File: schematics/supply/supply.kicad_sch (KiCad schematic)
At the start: 13 parts, among them J1 Conn_01x02_Pin, J2 Conn_01x02_Pin, J3 Conn_01x01_Pin, J4 Conn_01x01_Pin

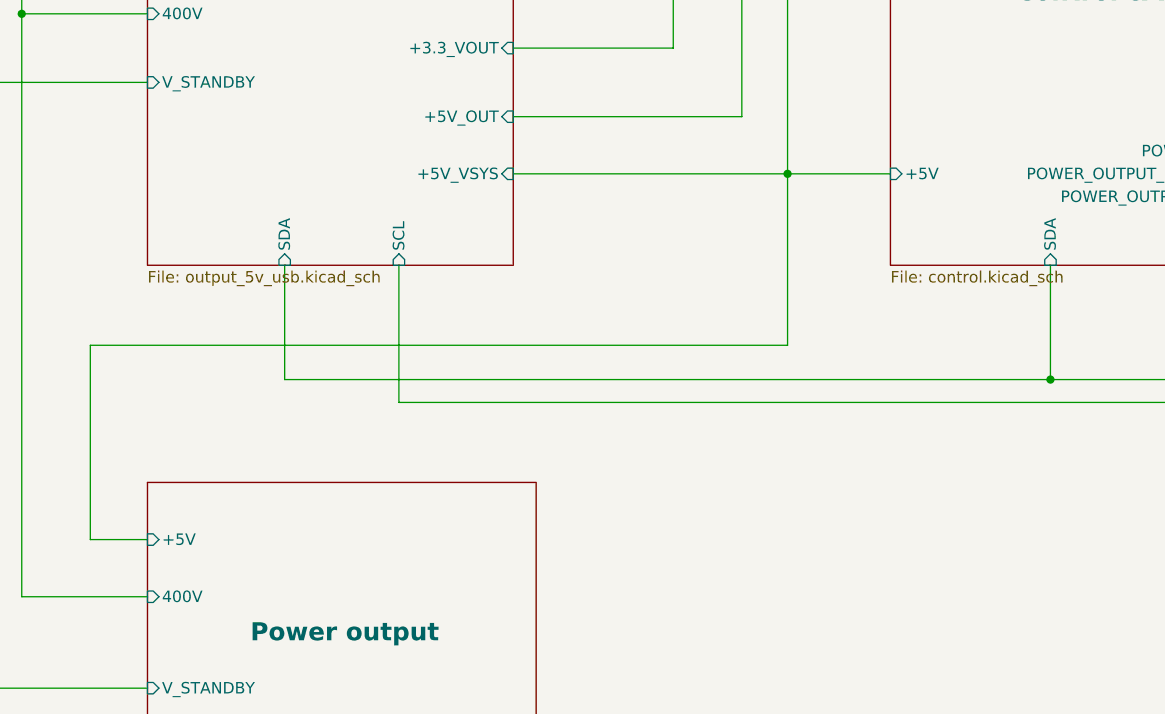
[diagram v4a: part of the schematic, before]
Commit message: Added over-voltage protection to 5V line
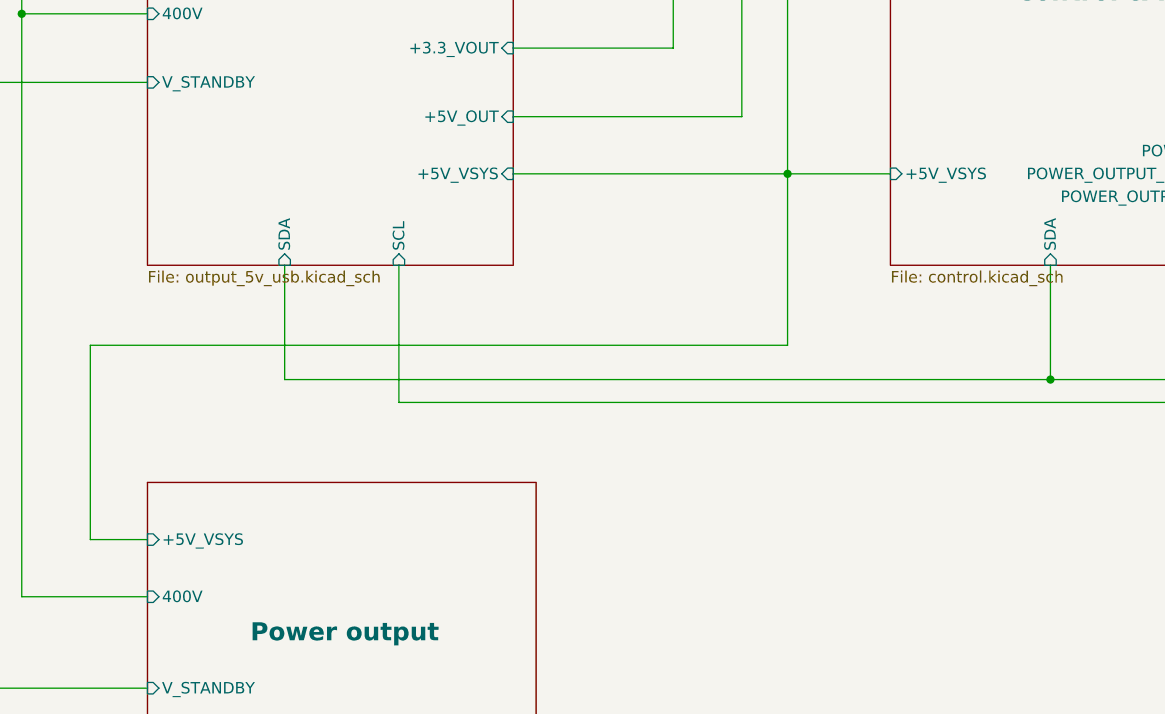
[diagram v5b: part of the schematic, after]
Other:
- sheet Control & Fan ports: added +5V_VSYS; removed +5V
- sheet Power output ports: added +5V_VSYS; removed +5V
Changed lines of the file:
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@@
-      (effects (font (size 1.27 1.27)) (justify left))
-    )
-    (pin "+5V" input (at 129.54 187.96 180)
       (effects (font (size 1.27 1.27)) (justify left))
     )
@@
     (pin "POWER_OUTPUT_FB" input (at 172.72 214.63 0)
       (effects (font (size 1.27 1.27)) (justify right))
+    )
+    (pin "+5V_VSYS" input (at 129.54 187.96 180)
+      (effects (font (size 1.27 1.27)) (justify left))
     )
     (instances
@@
       (effects (font (size 1.27 1.27)) (justify left))
     )
-    (pin "+5V" input (at 212.09 147.32 180)
-      (effects (font (size 1.27 1.27)) (justify left))
-    )
     (pin "SIGNAL_OUT" input (at 259.08 142.24 0)
       (effects (font (size 1.27 1.27)) (justify right))
@@
       (effects (font (size 1.27 1.27)) (justify right))
     )
+    (pin "+5V_VSYS" input (at 212.09 147.32 180)
+      (effects (font (size 1.27 1.27)) (justify left))
+    )
     (instances

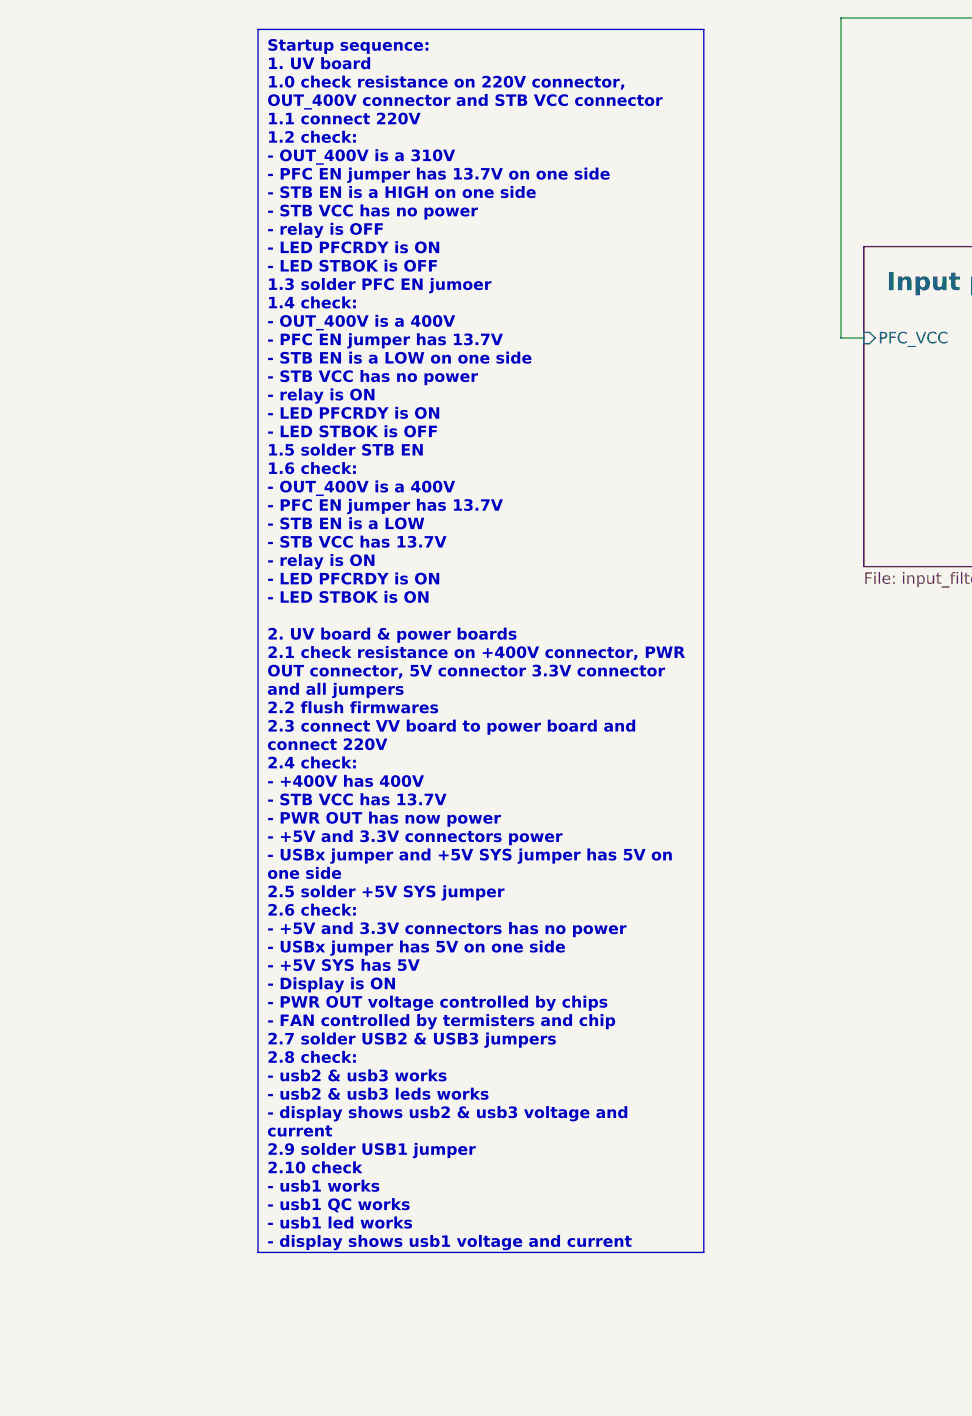
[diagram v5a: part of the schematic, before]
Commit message: Fixed problem with 20V on one leg of comparator
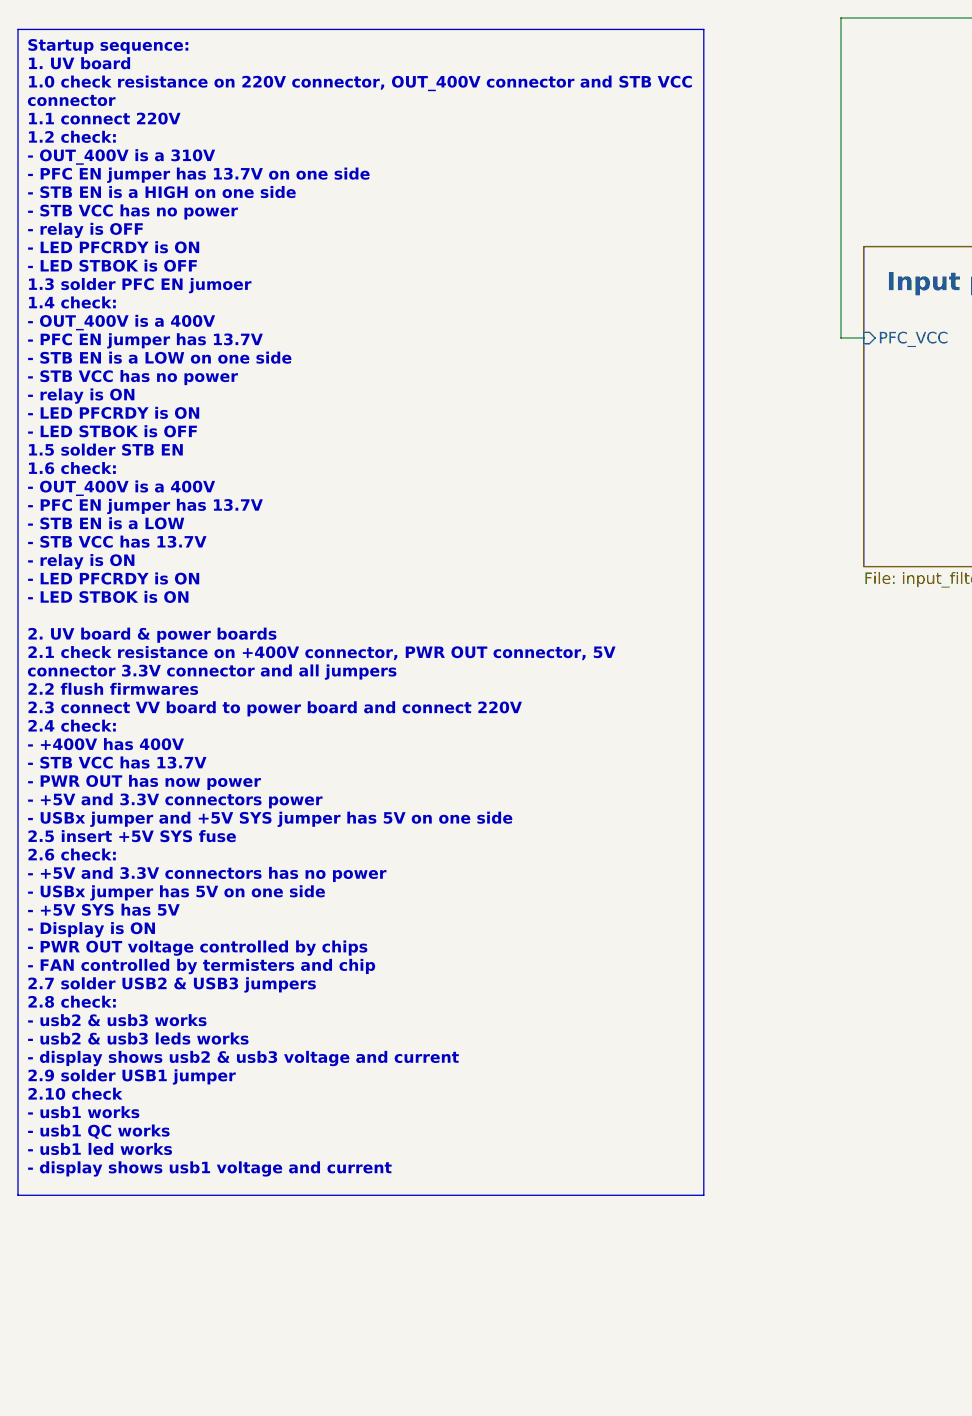
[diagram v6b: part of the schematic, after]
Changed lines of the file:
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@@
     (stroke (width 0) (type default))
   )
-  (text_box "Startup sequence:\n1. UV board\n1.0 check resistance on 220V connector, OUT_400V connector and STB VCC connector\n1.1 connect 220V\n1.2 check: \n    - OUT_400V is a 310V\n    - PFC EN jumper has 13.7V on one side \n    - STB EN is a HIGH on one side\n    - STB VCC has no power\n    - relay is OFF\n    - LED PFCRDY is ON\n    - LED STBOK is OFF\n1.3 solder PFC EN jumoer\n1.4 check:\n    - OUT_400V is a 400V\n    - PFC EN jumper has 13.7V\n    - STB EN is a LOW on one side\n    - STB VCC has no power\n    - relay is ON\n    - LED PFCRDY is ON\n    - LED STBOK is OFF\n1.5 solder STB EN\n1.6 check:\n    - OUT_400V is a 400V\n    - PFC EN jumper has 13.7V\n    - STB EN is a LOW\n    - STB VCC has 13.7V\n    - relay is ON\n    - LED PFCRDY is ON\n    - LED STBOK is ON\n\n2. UV board & power boards\n2.1 check resistance on +400V connector, PWR OUT connector, 5V connector 3.3V connector and all jumpers\n2.2 flush firmwares\n2.3 connect VV board to power board and connect 220V\n2.4 check:\n    - +400V has 400V\n    - STB VCC has 13.7V\n    - PWR OUT has now power\n    - +5V and 3.3V connectors power\n    - USBx jumper and +5V SYS jumper has 5V on one side\n2.5 solder +5V SYS jumper\n2.6 check:\n    - +5V and 3.3V connectors has no power\n    - USBx jumper has 5V on one side\n    - +5V SYS has 5V\n    - Display is ON\n    - PWR OUT voltage controlled by chips\n    - FAN controlled by termisters and chip\n2.7 solder USB2 & USB3 jumpers\n2.8 check: \n    - usb2 & usb3 works\n    - usb2 & usb3 leds works\n    - display shows usb2 & usb3 voltage and current\n2.9 solder USB1 jumper\n2.10 check \n    - usb1 works\n    - usb1 QC works\n    - usb1 led works\n    - display shows usb1 voltage and current\n"
-    (at -48.26 30.48 0) (size 49.53 135.89)
+  (text_box "Startup sequence:\n1. UV board\n1.0 check resistance on 220V connector, OUT_400V connector and STB VCC connector\n1.1 connect 220V\n1.2 check: \n    - OUT_400V is a 310V\n    - PFC EN jumper has 13.7V on one side \n    - STB EN is a HIGH on one side\n    - STB VCC has no power\n    - relay is OFF\n    - LED PFCRDY is ON\n    - LED STBOK is OFF\n1.3 solder PFC EN jumoer\n1.4 check:\n    - OUT_400V is a 400V\n    - PFC EN jumper has 13.7V\n    - STB EN is a LOW on one side\n    - STB VCC has no power\n    - relay is ON\n    - LED PFCRDY is ON\n    - LED STBOK is OFF\n1.5 solder STB EN\n1.6 check:\n    - OUT_400V is a 400V\n    - PFC EN jumper has 13.7V\n    - STB EN is a LOW\n    - STB VCC has 13.7V\n    - relay is ON\n    - LED PFCRDY is ON\n    - LED STBOK is ON\n\n2. UV board & power boards\n2.1 check resistance on +400V connector, PWR OUT connector, 5V connector 3.3V connector and all jumpers\n2.2 flush firmwares\n2.3 connect VV board to power board and connect 220V\n2.4 check:\n    - +400V has 400V\n    - STB VCC has 13.7V\n    - PWR OUT has now power\n    - +5V and 3.3V connectors power\n    - USBx jumper and +5V SYS jumper has 5V on one side\n2.5 insert +5V SYS fuse\n2.6 check:\n    - +5V and 3.3V connectors has no power\n    - USBx jumper has 5V on one side\n    - +5V SYS has 5V\n    - Display is ON\n    - PWR OUT voltage controlled by chips\n    - FAN controlled by termisters and chip\n2.7 solder USB2 & USB3 jumpers\n2.8 check: \n    - usb2 & usb3 works\n    - usb2 & usb3 leds works\n    - display shows usb2 & usb3 voltage and current\n2.9 solder USB1 jumper\n2.10 check \n    - usb1 works\n    - usb1 QC works\n    - usb1 led works\n    - display shows usb1 voltage and current\n"
+    (at -74.93 30.48 0) (size 76.2 129.54)
     (stroke (width 0) (type default))
     (fill (type none))

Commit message: Some changes in board - Im preparing it to production
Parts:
- added H1: MountingHole, MountingHole:MountingHole_2.2mm_M2, symbol Mechanical:MountingHole
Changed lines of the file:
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@@
       (project "supply"
         (path "/1e139717-fcd1-4008-a6ea-4c993845e928"
-          (reference "H3") (unit 1)
+          (reference "H4") (unit 1)
         )
       )
@@
       (project "supply"
         (path "/1e139717-fcd1-4008-a6ea-4c993845e928"
-          (reference "H1") (unit 1)
+          (reference "H2") (unit 1)
         )
       )
@@
       (project "supply"
         (path "/1e139717-fcd1-4008-a6ea-4c993845e928"
-          (reference "H5") (unit 1)
+          (reference "H6") (unit 1)
         )
       )
@@
       (project "supply"
         (path "/1e139717-fcd1-4008-a6ea-4c993845e928"
-          (reference "H6") (unit 1)
+          (reference "H7") (unit 1)
         )
       )
@@
     )
   )
+  (symbol (lib_id "Mechanical:MountingHole") (at 31.75 231.14 0) (unit 1)
+    (in_bom yes) (on_board yes) (dnp no) (fields_autoplaced)
+    (property "Reference" "H1" (at 34.29 229.8699 0)
+      (effects (font (size 1.27 1.27)) (justify left))
+    )
+    (property "Value" "MountingHole" (at 34.29 232.4099 0)
+      (effects (font (size 1.27 1.27)) (justify left))
+    )
+    (property "Footprint" "MountingHole:MountingHole_2.2mm_M2" (at 31.75 231.14 0)
+      (effects (font (size 1.27 1.27)) hide)
+    )
+    (property "Datasheet" "~" (at 31.75 231.14 0)
+      (effects (font (size 1.27 1.27)) hide)
+    )
+    (instances
+      (project "xray"
+        (path "/002cc585-3681-421a-8dca-b0910197d82b"
+          (reference "H1") (unit 1)
+        )
+      )
+      (project "supply"
+        (path "/1e139717-fcd1-4008-a6ea-4c993845e928"
+          (reference "H1") (unit 1)
+        )
+      )
+    )
+  )
   (symbol (lib_id "Mechanical:MountingHole") (at 31.75 246.38 0) (unit 1)
     (in_bom yes) (on_board yes) (dnp no) (fields_autoplaced)
@@
       (project "supply"
         (path "/1e139717-fcd1-4008-a6ea-4c993845e928"
-          (reference "H2") (unit 1)
+          (reference "H3") (unit 1)
         )
       )
@@
       (project "supply"
         (path "/1e139717-fcd1-4008-a6ea-4c993845e928"
-          (reference "H7") (unit 1)
+          (reference "H8") (unit 1)
         )
       )
@@
       (project "supply"
         (path "/1e139717-fcd1-4008-a6ea-4c993845e928"
-          (reference "H4") (unit 1)
+          (reference "H5") (unit 1)
         )
       )
@@
       (project "supply"
         (path "/1e139717-fcd1-4008-a6ea-4c993845e928"
-          (reference "H9") (unit 1)
+          (reference "H10") (unit 1)
         )
       )
@@
       (project "supply"
         (path "/1e139717-fcd1-4008-a6ea-4c993845e928"
-          (reference "H8") (unit 1)
-        )
-      )
+          (reference "H9") (unit 1)
+        )
+      )

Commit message: Changed fuse on 400V line
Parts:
- H1: now left out of the parts list
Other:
- note added: "Holes on board#1"
- note added: "Holes on board#2"
- moved on the sheet: J1, J2, J3, J4
